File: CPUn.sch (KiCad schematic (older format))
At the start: 21 parts, among them J4 JTAG

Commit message: Squiggles! Silk!
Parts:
- renumbered C162 to C501, C163 to C502, C164 to C503, C165 to C504, C166 to C505, C167 to C506, C168 to C507, C169 to C508, C170 to C509, C171 to C510, C76 to C511, C75 to C512, J4 to J501, R105 to R501, R108 to R502, R109 to R503, R98 to R504, R99 to R505, R117 to R506

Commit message: Final BOM
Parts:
- R501: value 330 -> 750; BOM RES SMD 330 1% [0402] -> RES SMD 750 [0402]
- R504, R505: value 5k1 -> 4k3; BOM RES SMD 5k1 1% [0402] -> RES SMD 4k3 [0402]

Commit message: Redecoupling
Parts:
- removed C501, C502, C503, C504, C505, C506, C507, C508, C509, C510: 1u, IPC7351-Nominal:CAPC1005X55, symbol C-0402
- removed CPU0: XC6SLX25-FGG484, manuf:XILINX-FGG484, symbol XC6SLX25-FGG484
- added C501, C502, C503, C504, C505, C506, C507, C508, C509, C510, C513, C514, C515, C516, C517, C518, C519, C520, C521, C522, C523, C524, C525, C526, C527, C528, C529, C530, C531, C532, C533, C534, C535, C536, C537, C538, C539, C540, C541, C542, C543, C544, C545, C546, C547, C548, C549: 100n, IPC7351-Nominal:CAPC0603X33, symbol C-0201
- added C650, C651, C652, C653: 22u, IPC7351-Nominal:CAPC2012X70, symbol C-0805
- added CPU0: XC6SLX45-FGG484, manuf:XILINX-FGG484, symbol XC6SLX45-FGG484
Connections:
- wire segments 244 -> 359
- no-connect marks 177 -> 3
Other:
- moved on the sheet: C611, C612, CACHE1, J601, R601, R602, R603, R604, R605, R606

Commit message: Fix more shit for to pass ERC
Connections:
- no-connect marks 3 -> 227

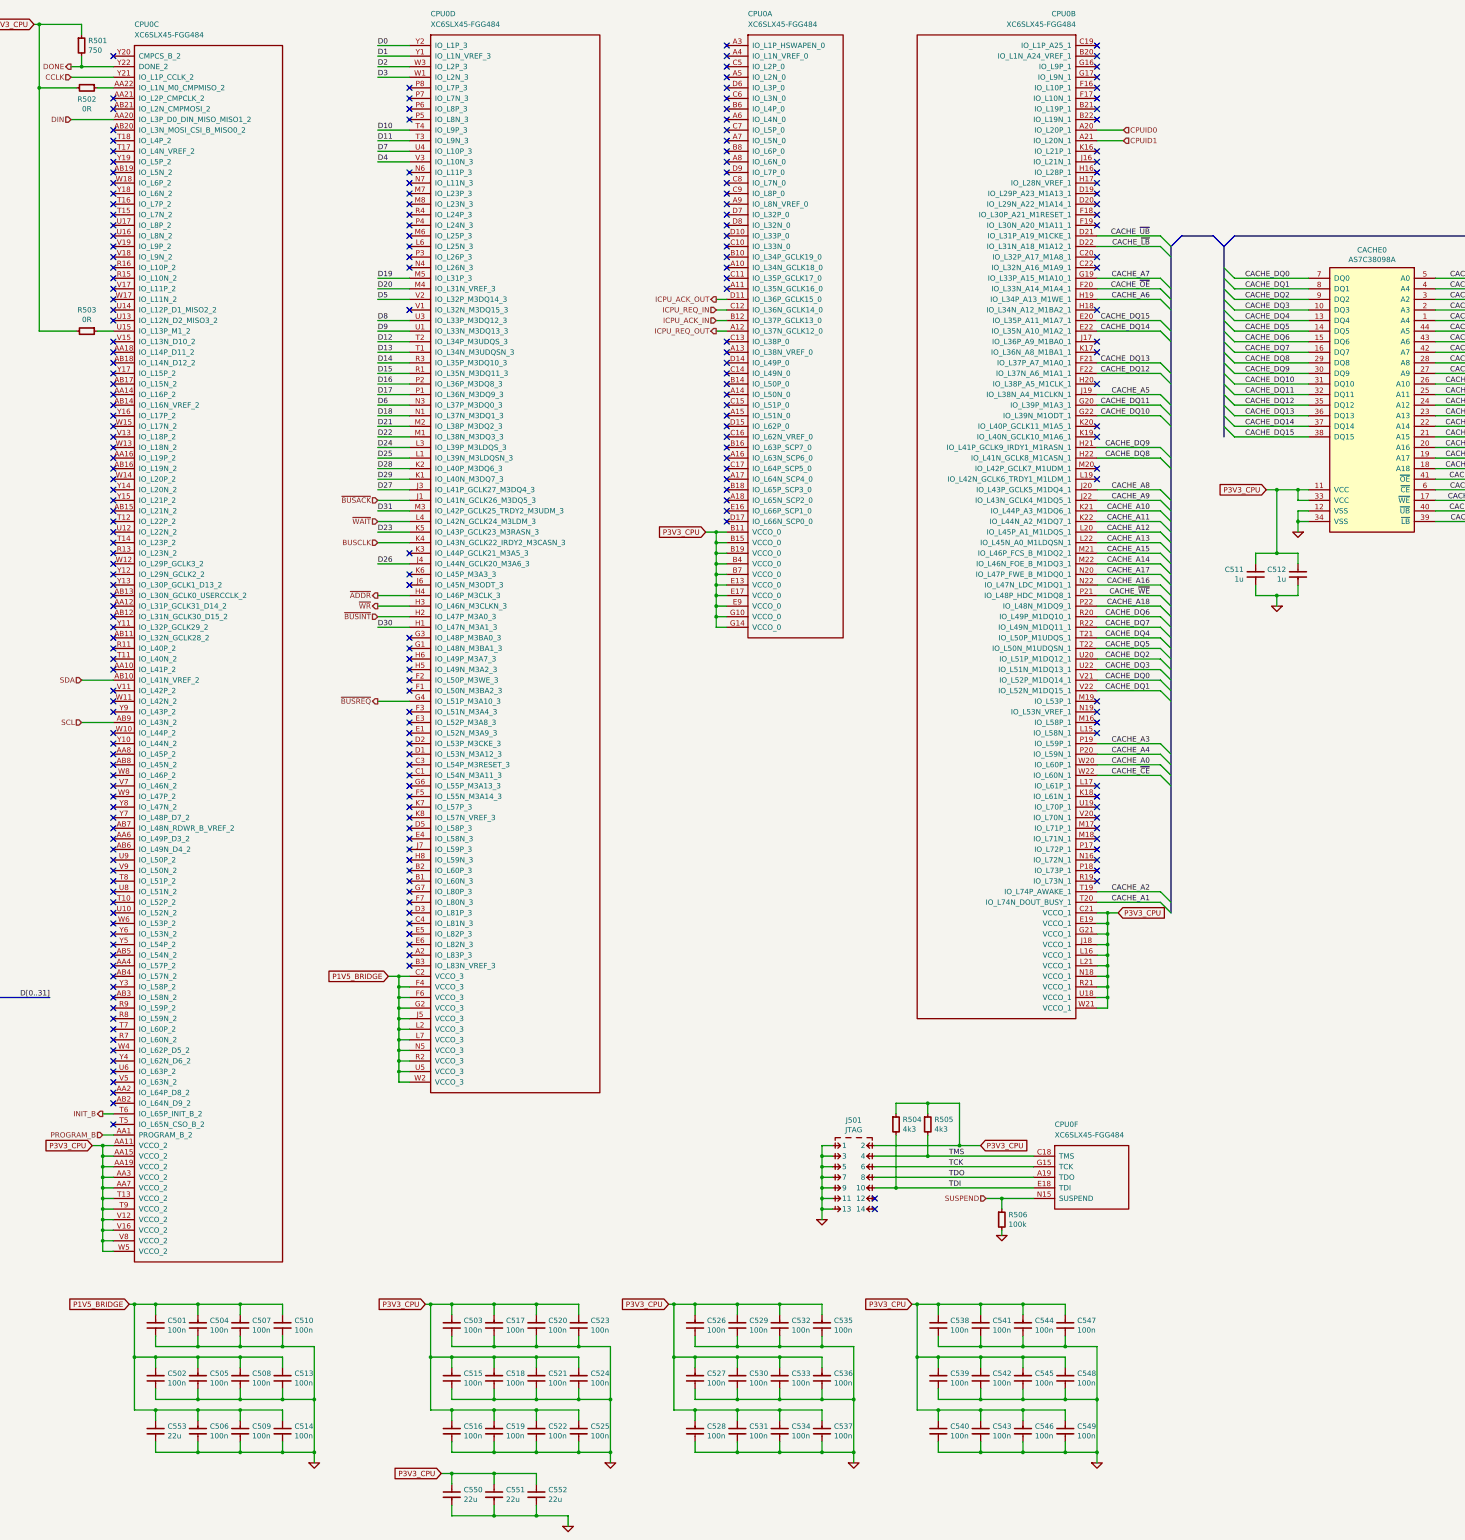
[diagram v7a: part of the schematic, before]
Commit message: Add power input protection
- Add a fast-blow 6A fuse
- Specify an optional slow-blow if the fast-blow blows
- Add snubber near input to damp resonances and prevent spikes
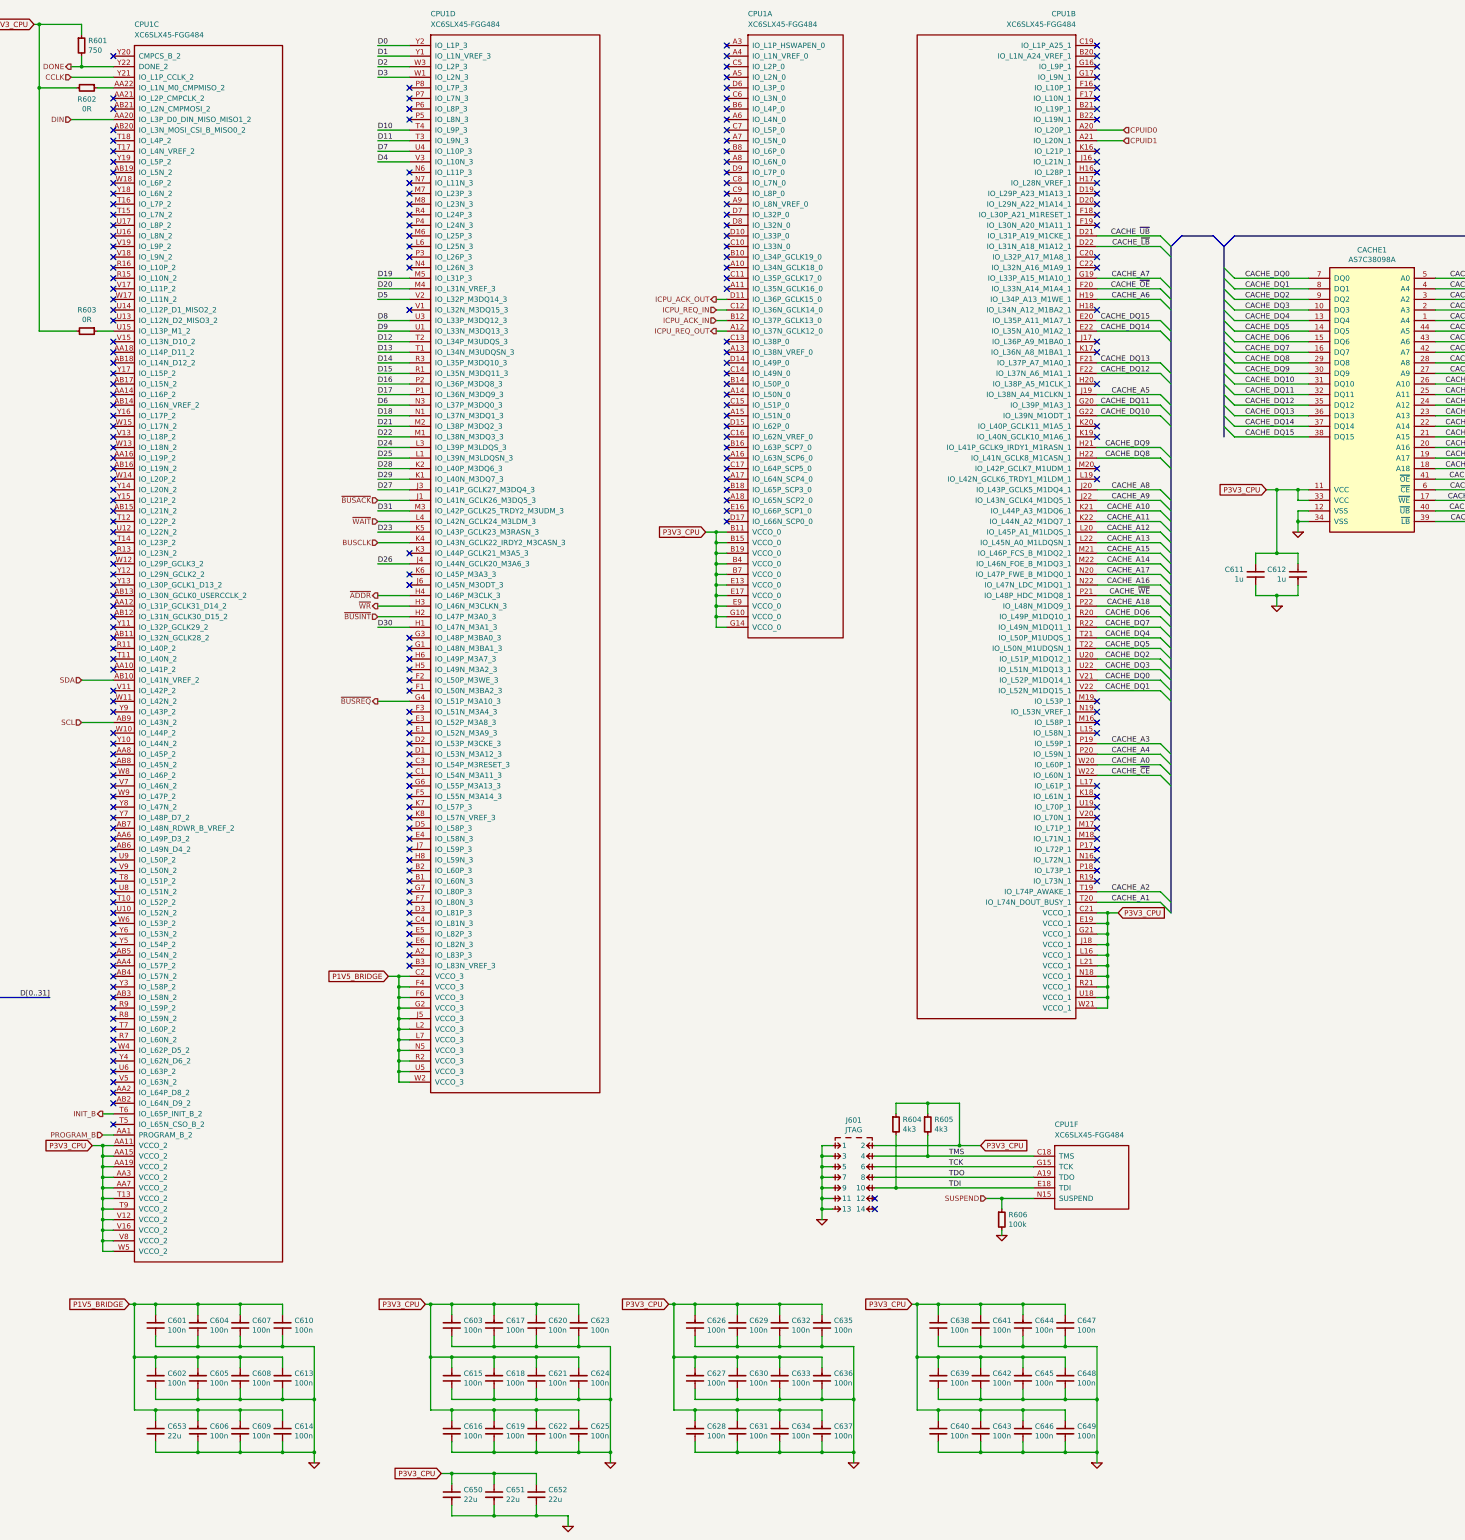
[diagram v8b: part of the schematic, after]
